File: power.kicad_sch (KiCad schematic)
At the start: 55 parts

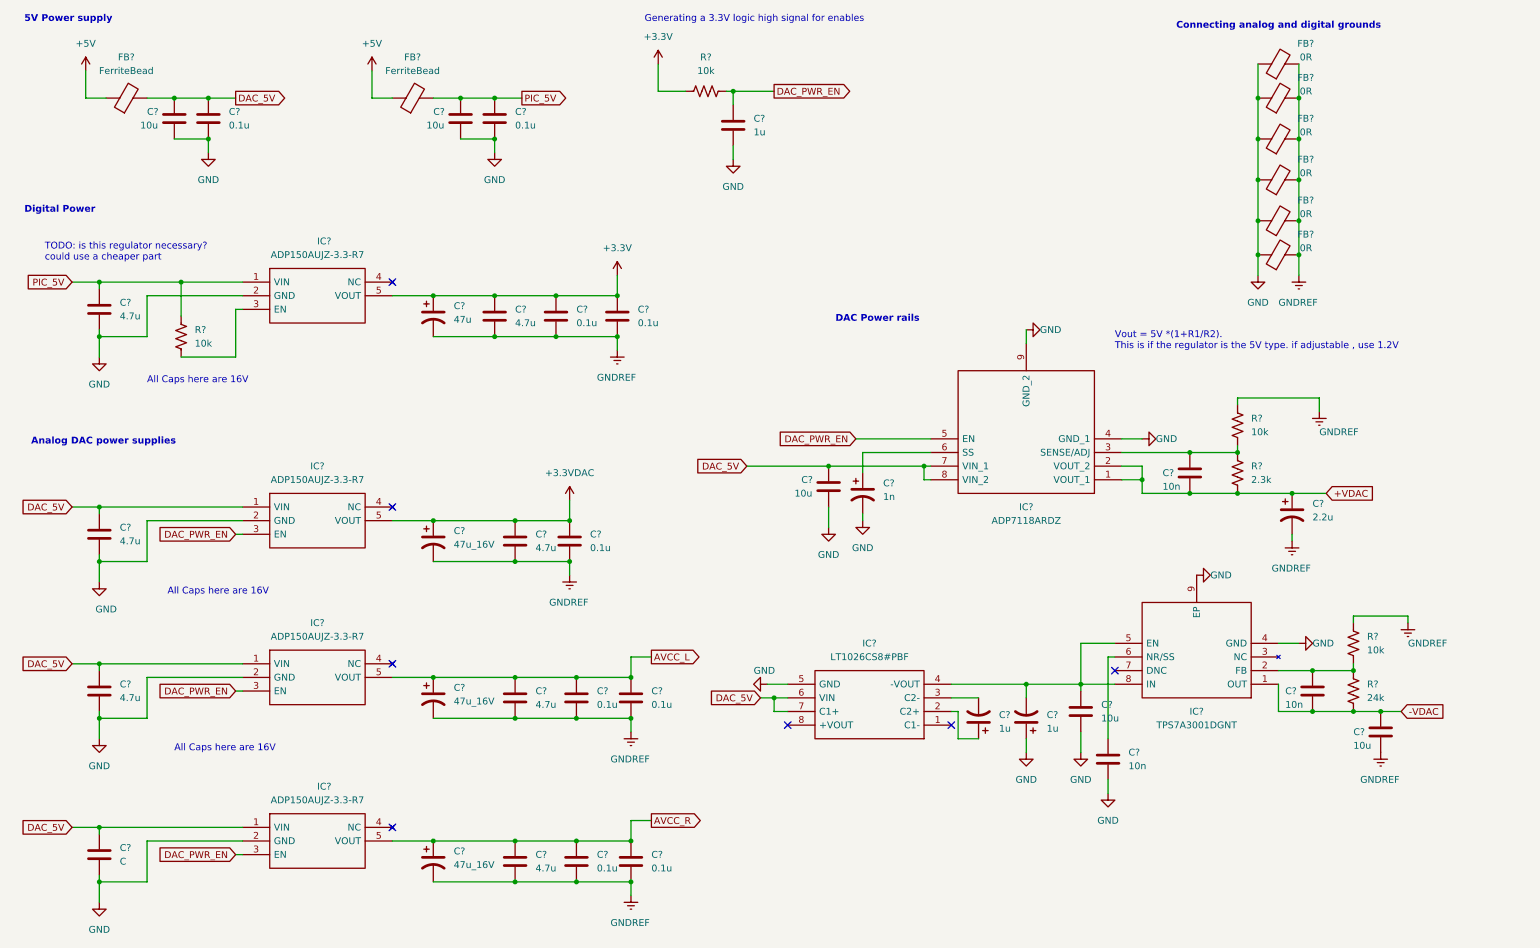
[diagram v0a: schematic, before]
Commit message: Finishing Schematic. Fixed ERC errors
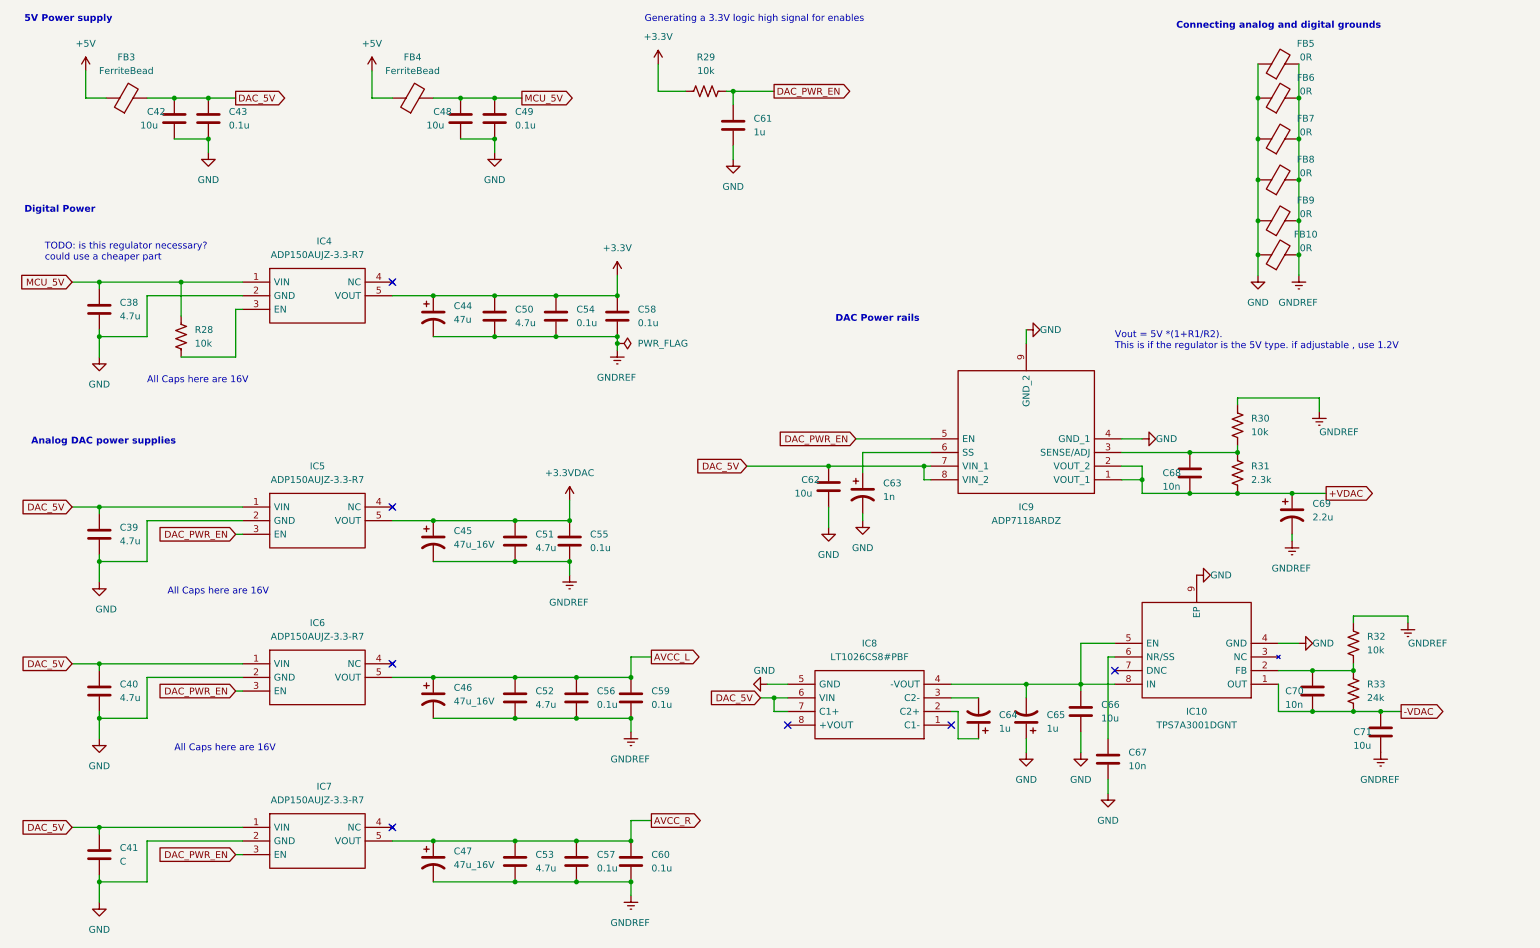
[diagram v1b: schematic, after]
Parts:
- gave numbers to parts that had none: 55
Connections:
- net PIC_5V renamed MCU_5V

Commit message: Adding footprints
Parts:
- C38, C39, C40, C41, C42, C43, C44, C45, C46, C47, C48, C49, C50, C51, C52, C53, C54, C55, C56, C57, C58, C59, C60, C61, C62, C63, C64, C65, C66, C67, C68, C69, C70, C71: footprint (none) -> Capacitor_SMD:C_0805_2012Metric_Pad1.18x1.45mm_HandSolder
- IC10: footprint SOP65P490X110-9N -> SamacSys_Parts:SOP65P490X110-9N
- IC4, IC5, IC6, IC7: footprint SOT95P280X100-5N -> SamacSys_Parts:SOT95P280X100-5N
- IC8: footprint SOIC127P599X175-8N -> SamacSys_Parts:SOIC127P599X175-8N
- IC9: footprint SOIC127P600X175-9N -> SamacSys_Parts:SOIC127P600X175-9N
- R28, R29, R30, R31, R32, R33: footprint (none) -> Resistor_SMD:R_0805_2012Metric_Pad1.20x1.40mm_HandSolder

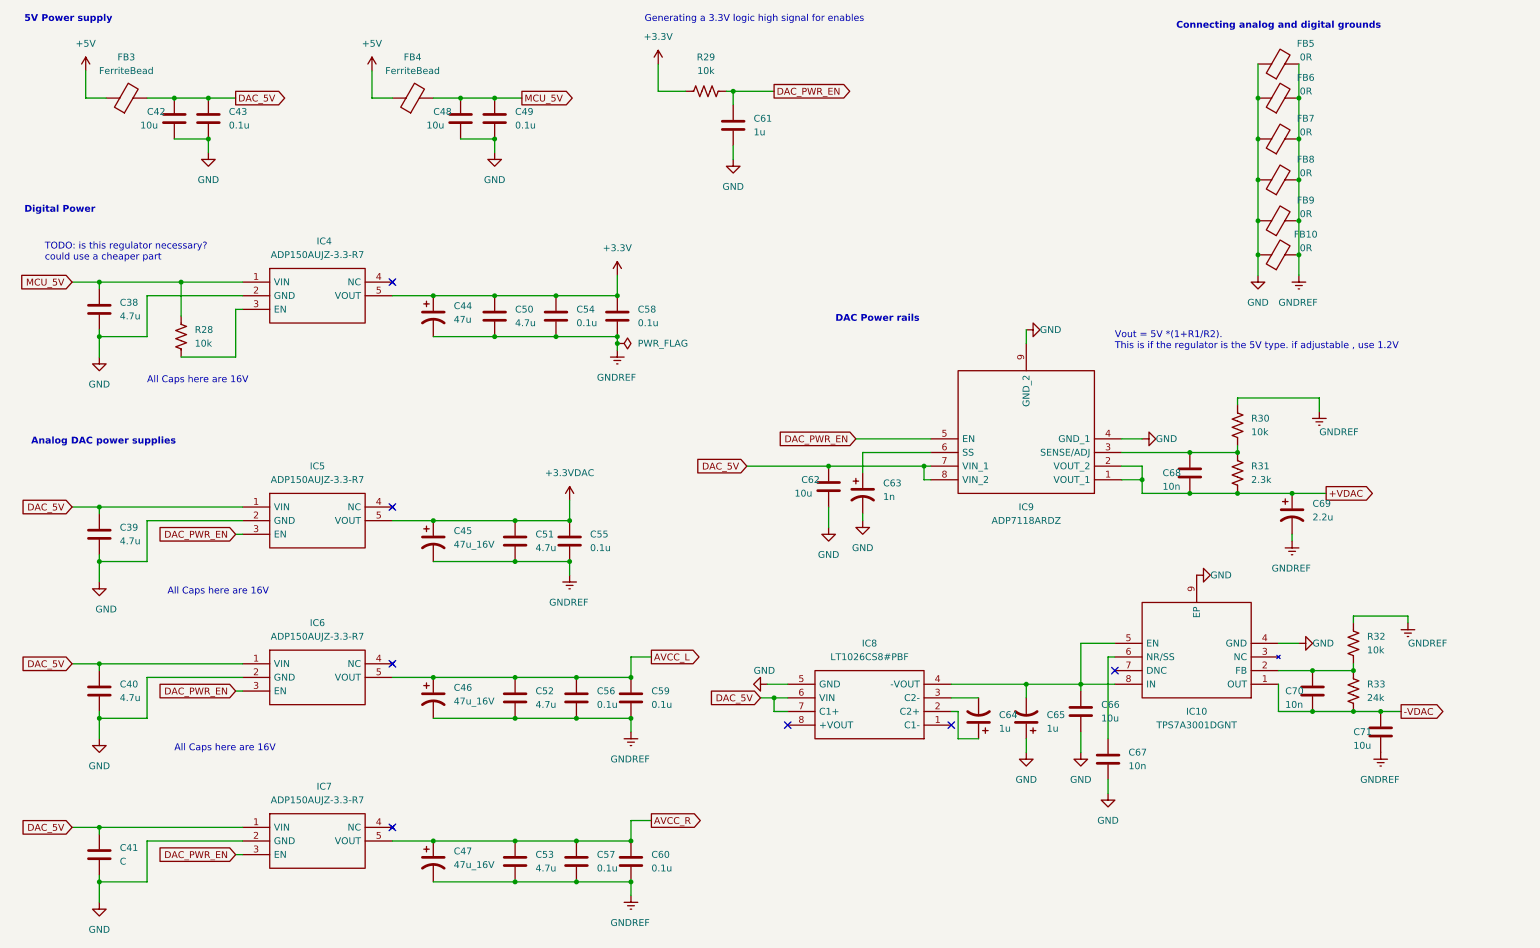
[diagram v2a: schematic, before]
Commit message: Adding footprints. WIP PCB, finished routing, no ground planes yet
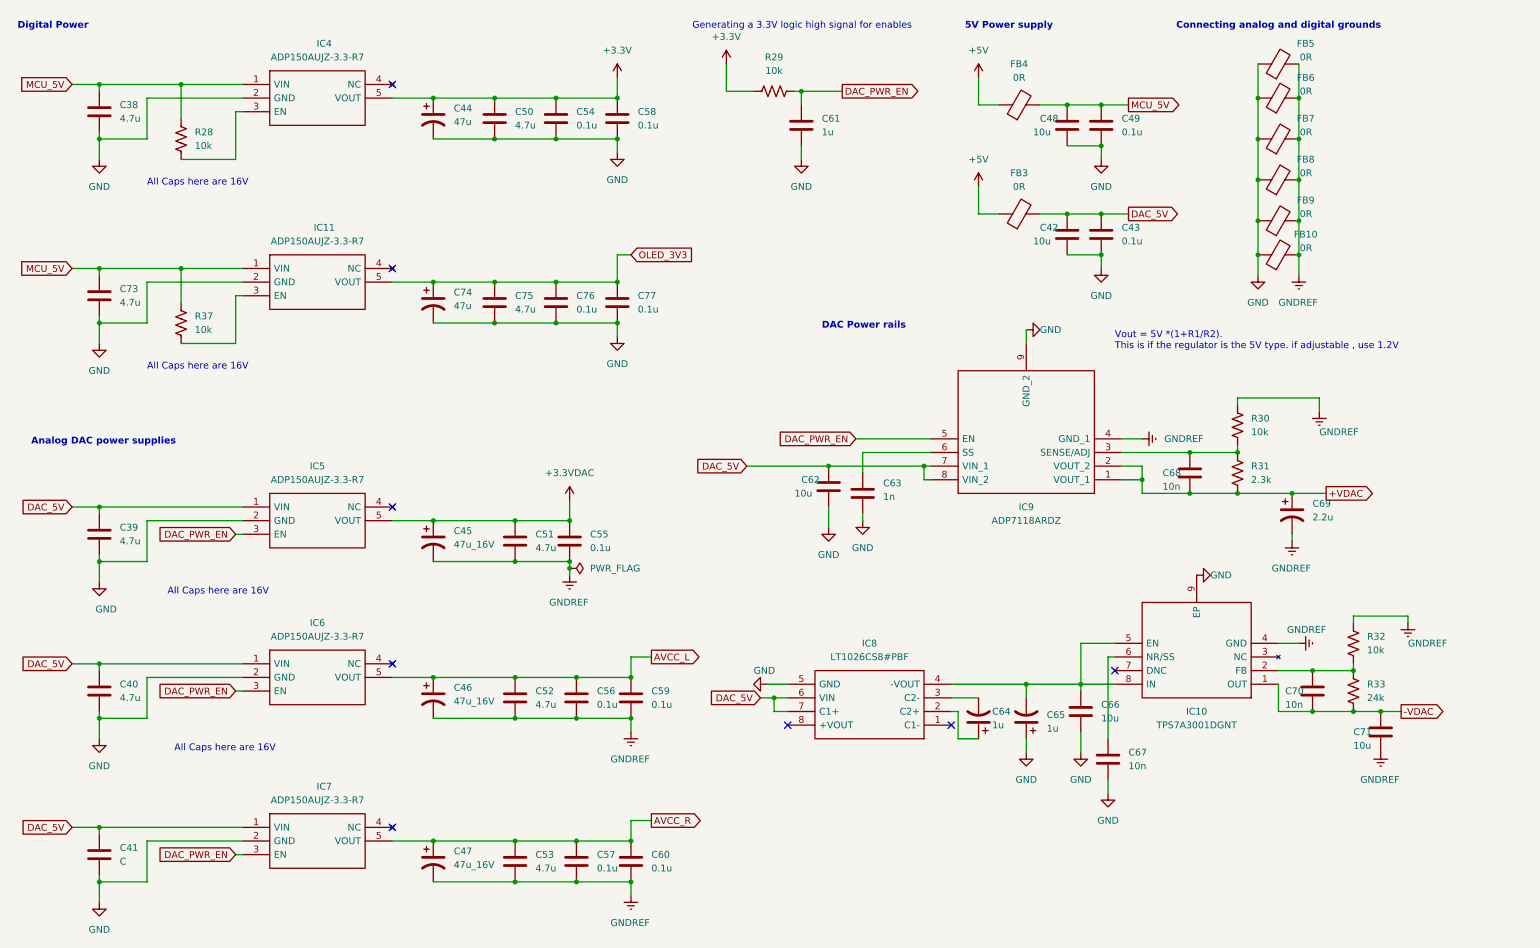
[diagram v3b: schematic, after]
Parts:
- added C73, C75: 4.7u, Capacitor_SMD:C_0805_2012Metric_Pad1.18x1.45mm_HandSolder, symbol Device:C
- added C74: 47u, Capacitor_THT:CP_Radial_D5.0mm_P2.50mm, symbol Device:C_Polarized_US
- added C76, C77: 0.1u, Capacitor_SMD:C_0805_2012Metric_Pad1.18x1.45mm_HandSolder, symbol Device:C
- added IC11: ADP150AUJZ-3.3-R7, SamacSys_Parts:SOT95P280X100-5N, symbol SamacSys_Parts:ADP150AUJZ-3.3-R7
- added R37: 10k, Resistor_SMD:R_0805_2012Metric_Pad1.20x1.40mm_HandSolder, symbol Device:R_US
- C44, C45, C46, C47: footprint Capacitor_SMD:C_0805_2012Metric_Pad1.18x1.45mm_HandSolder -> Capacitor_THT:CP_Radial_D5.0mm_P2.50mm; Mouser Part Number (none) -> 667-ECA-1CHG470I; Part Number (none) -> ECA-1CHG470I
- C63: symbol Device:C_Polarized_US -> Device:C
- C64, C65: footprint Capacitor_SMD:C_0805_2012Metric_Pad1.18x1.45mm_HandSolder -> Capacitor_THT:CP_Radial_D5.0mm_P2.00mm; Mouser Part Number (none) -> 80-ESH105M100AC3AA; Part Number (none) -> ESH105M100AC3AA
- C69: footprint Capacitor_SMD:C_0805_2012Metric_Pad1.18x1.45mm_HandSolder -> Capacitor_THT:CP_Radial_D4.0mm_P1.50mm; Mouser Part Number (none) -> 667-ECE-A1HKA2R2; Part Number (none) -> ECE-A1HKA2R2
- FB10, FB5, FB6, FB7, FB8, FB9: footprint (none) -> SamacSys_Parts:BEADC2012X110N
- FB3, FB4: value FerriteBead -> 0R; footprint (none) -> SamacSys_Parts:BEADC2012X110N
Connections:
- net GND: now also C44.2, C50.2, C54.2, C58.2, C73.2, C74.2, C75.2, C76.2, C77.2, IC11.2 (GND); no longer IC10.4 (GND), IC9.4 (GND_1)
- net GNDREF: now also IC10.4 (GND), IC9.4 (GND_1); no longer C44.2, C50.2, C54.2, C58.2
- net MCU_5V: now also C73.1, IC11.1 (VIN), R37.2
- new net: IC11.3 (EN), R37.1
- new net OLED_3V3: C74.1, C75.1, C76.1, C77.1, IC11.5 (VOUT)
- no-connect marks 7 -> 8
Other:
- note removed: "TODO: is this regulator necessary? could use a cheaper part"
- moved on the sheet: C38, C42, C43, C44, C48, C49, C50, C54, C58, C61, FB3, FB4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

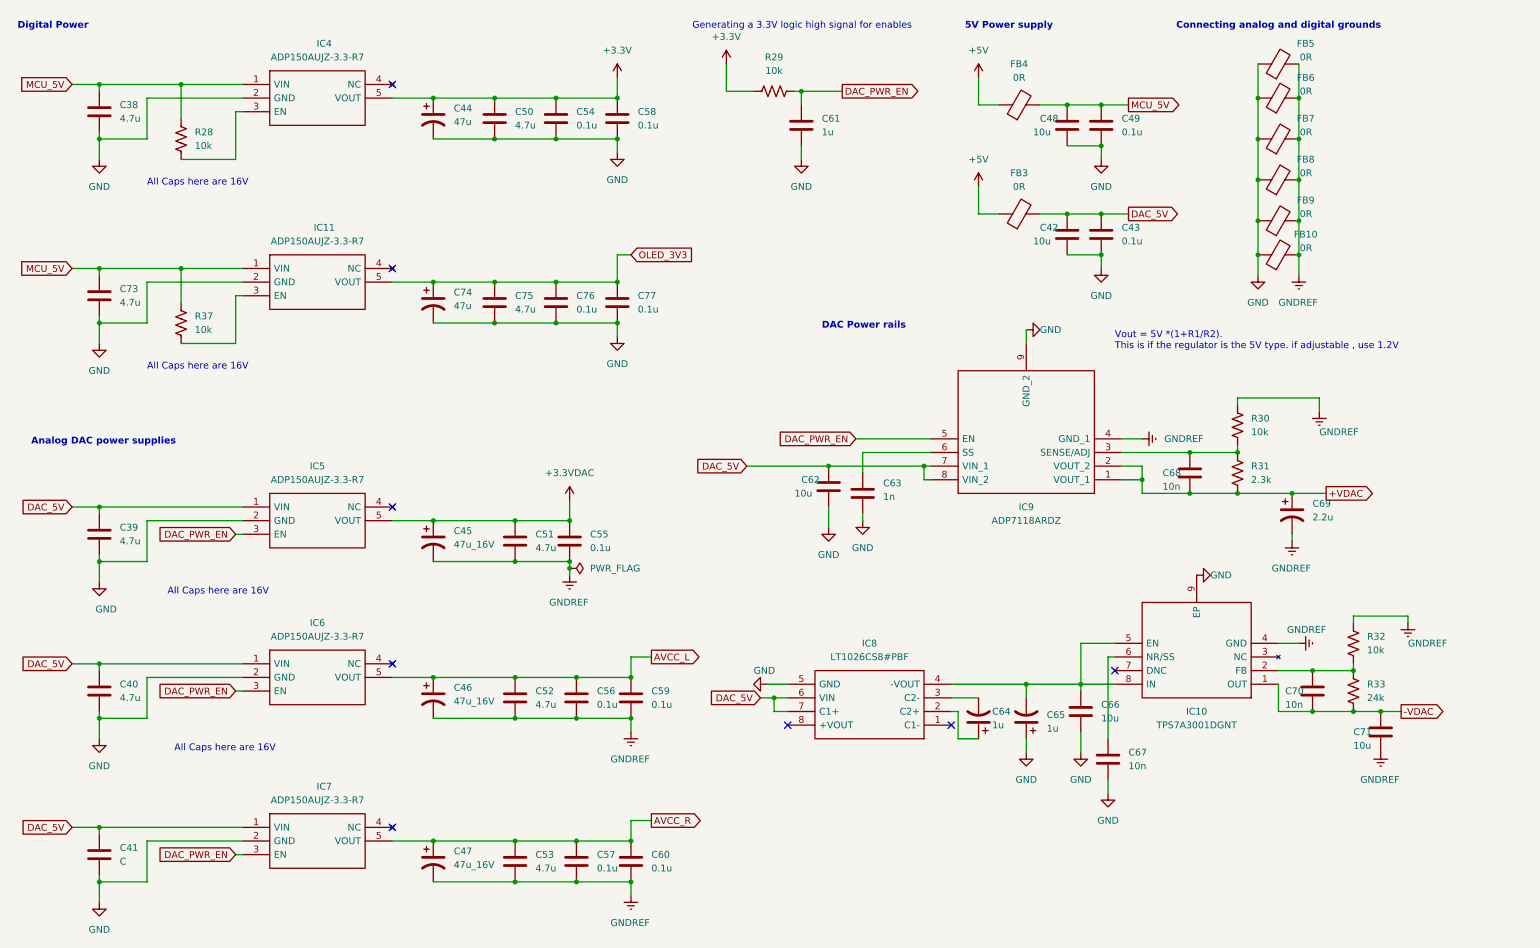
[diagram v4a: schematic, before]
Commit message: Adding part numbers for passives
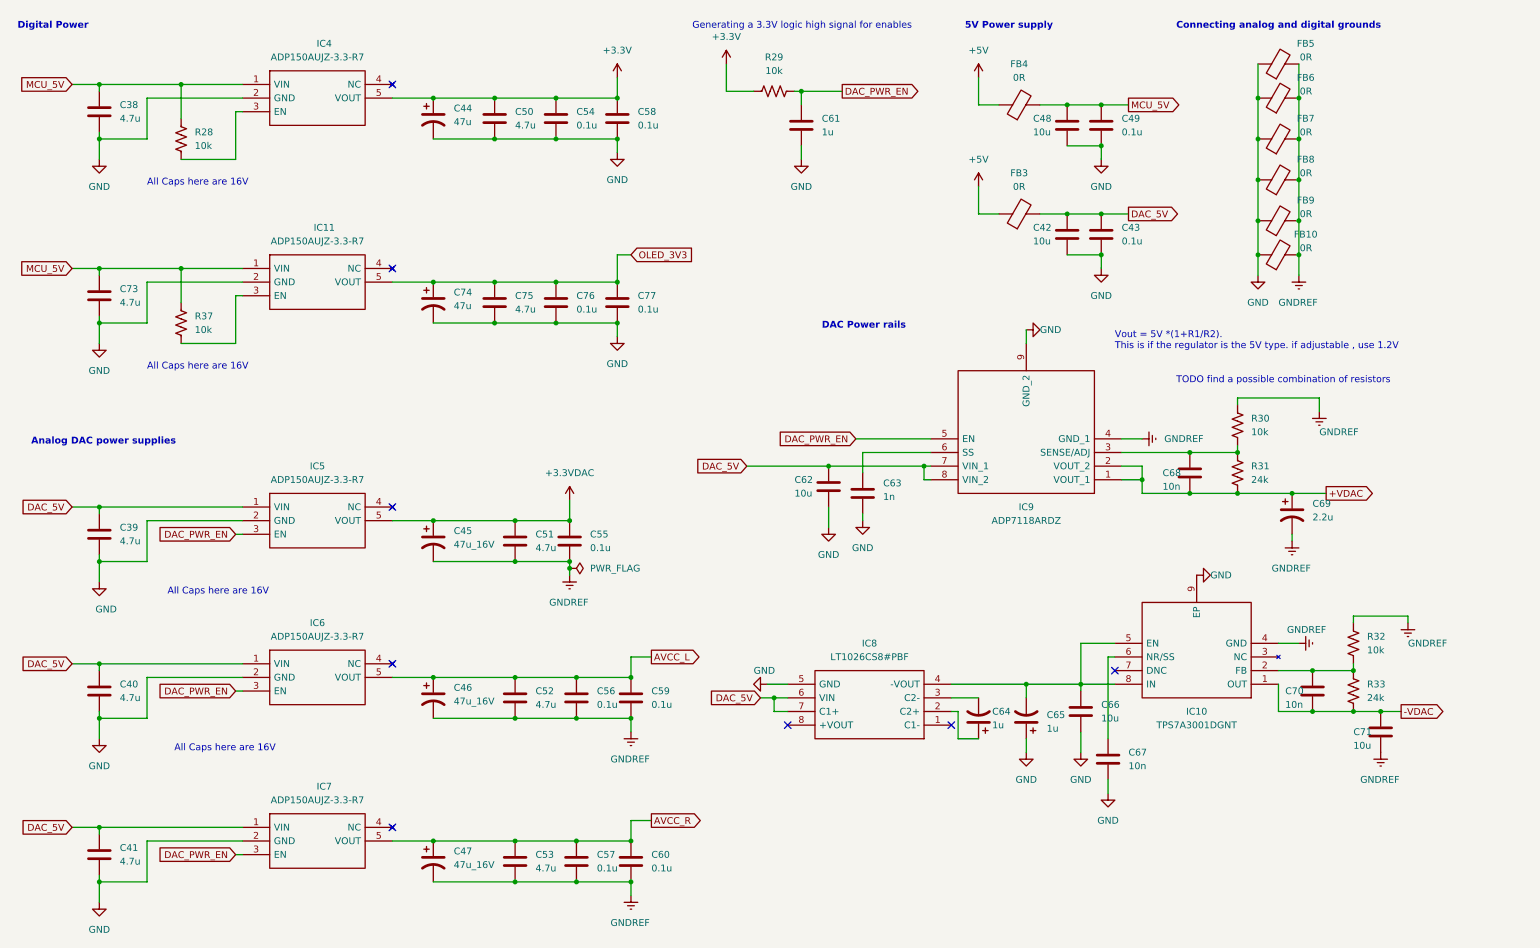
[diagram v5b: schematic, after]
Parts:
- C38, C39, C40, C51, C52, C53, C73, C75: Mouser Part Number (none) -> 80-C0805C104K8RAUTO; Part Number (none) -> C0805C104K8RACAUTO
- C41: value C -> 4.7u; Mouser Part Number (none) -> 80-C0805C104K8RAUTO; Part Number (none) -> C0805C104K8RACAUTO
- C42, C48, C62, C66: Mouser Part Number (none) -> 963-LMK212ABJ106KG8T; Part Number (none) -> LMK212ABJ106KG8T
- C43, C49, C54, C55, C56, C57, C58, C59, C60, C76, C77: Mouser Part Number (none) -> 187-CL21B104KBCNFNC; Part Number (none) -> CL21B104KBCNFNC
- C61: Mouser Part Number (none) -> 963-EMK212B7105KG-T; Part Number (none) -> EMK212B7105KG-T
- C63: Mouser Part Number (none) -> 581-0805YD102KAT2A; Part Number (none) -> 0805YD102KAT2A
- C67, C68, C70: Mouser Part Number (none) -> 80-C0805C103K4RECTU; Part Number (none) -> C0805C103K4RECTU
- FB10, FB3, FB4, FB5, FB6, FB7, FB8, FB9: Mouser Part Number (none) -> 704-MFBW1V2012-000-R; Part Number (none) -> MFBW1V2012-000-R
- R28, R29, R37: Mouser Part Number (none) -> 603-RC0805FR-7W10KL; Part Number (none) -> RC0805FR-7W10KL
- R30, R32: Mouser Part Number (none) -> 603-RT0805BRD0710KL; Part Number (none) -> RT0805BRD0710KL
- R31: value 2.3k -> 24k; Mouser Part Number (none) -> 667-ERA-6AEB243V; Part Number (none) -> ERA-6AEB243V
- R33: Mouser Part Number (none) -> 667-ERA-6AEB243V; Part Number (none) -> ERA-6AEB243V
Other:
- note added: "TODO find a possible combination of resistors"
